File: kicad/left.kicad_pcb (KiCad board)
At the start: 4 copper layers, 137.5 x 109.3 mm, 114 parts, among them Q1 PMF170XP,115, Q2 FS8205A_C2830320, SW1 TS-1088-AR02016, U1 SN74LVC1G17DBVR, U2 E73-2G4M08S1C, U3 SN74LVC1G74DQER, U4 S2B-PH-K-S(LF)(SN), U5 BL8573CS8TR, U6 DW01A_C42380662, U7 LP5024RSMR, U8 MAX17048, U9 USBLC6-2SC6, X1 FC-13532.768KHZ9PF20PPM

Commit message: rewired and finalized right side. updated panel. changed dnp of some components on both sides
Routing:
- net /COL1: track 230.3 -> 227.1 mm
- net GND: vias 320 -> 340

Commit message: fixed u9 to have pin 5 after polyfuse
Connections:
- U9 pad 5: /VBUS_RAW -> /VBUS
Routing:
- net /VBUS: track 71.7 -> 83.0 mm
- net /VBUS_RAW: track 25.6 -> 17.2 mm

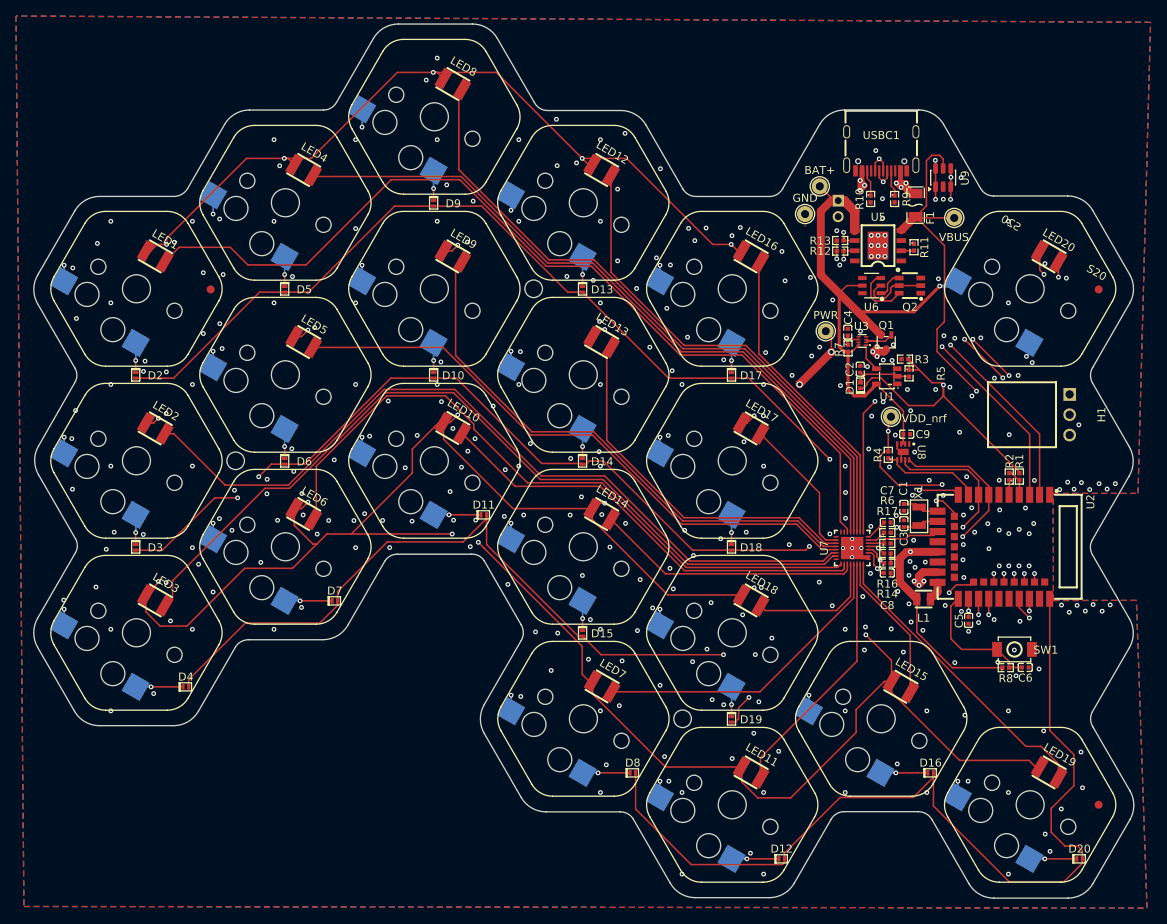
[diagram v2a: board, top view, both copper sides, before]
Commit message: plan for changing charger. reason = heat
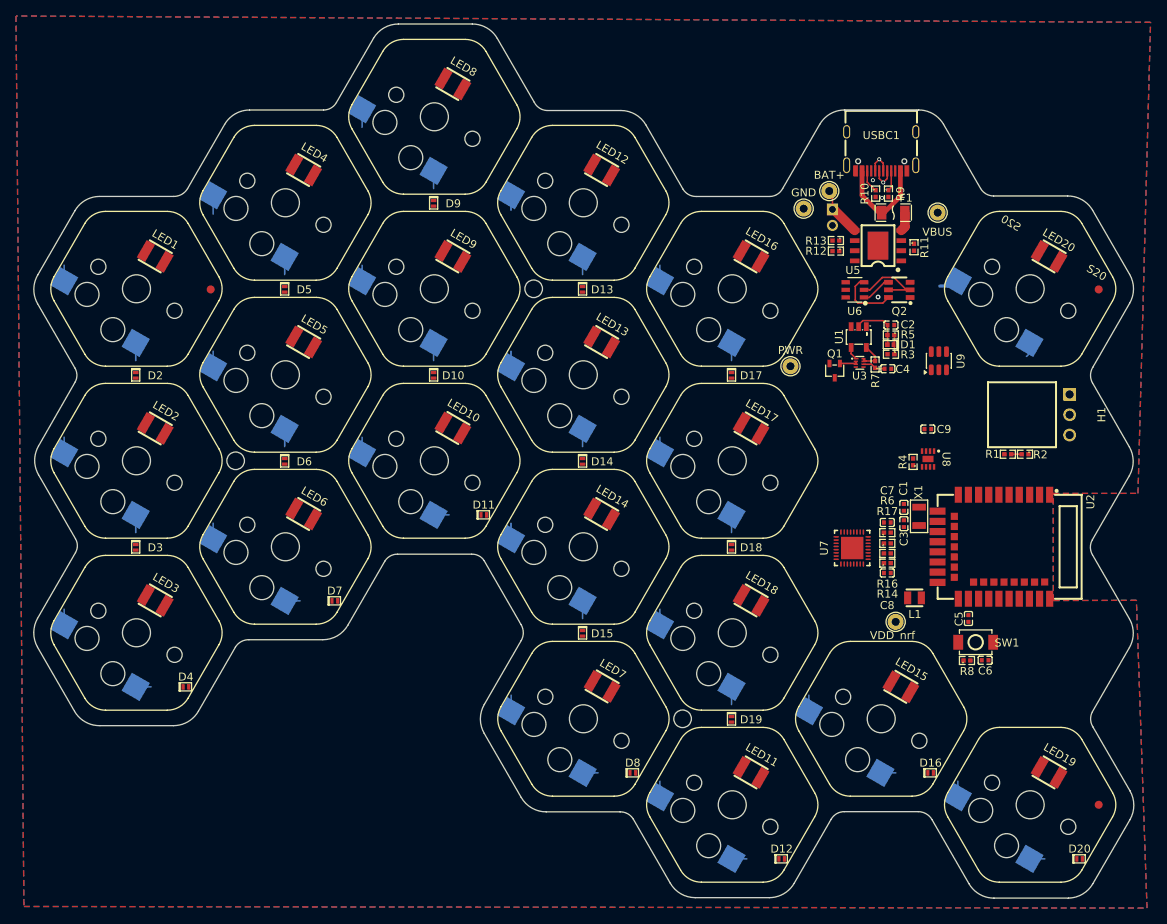
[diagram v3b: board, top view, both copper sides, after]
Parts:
- moved VDD_nrf 25.6 mm to (127.8, 90.5)
- moved U9 22.9 mm to (133.2, 57.9)
- moved Q1 7.35 mm to (120.2, 59.1)
- moved C4 6.78 mm to (126.8, 58.9), turned to 180 degrees
- moved C2 6.72 mm to (127.2, 53.4), turned to 0 degrees
- moved D1 6.30 mm to (127.1, 55.9), turned to 180 degrees
- moved PWR 6.22 mm to (114.6, 58.6)
- moved U1 6.04 mm to (123.2, 54.9), turned to 90 degrees
- moved R5 5.30 mm to (127.2, 54.7), turned to 180 degrees
- moved C6 5.09 mm to (139.0, 95.4)
- moved R8 4.94 mm to (136.7, 95.4)
- moved SW1 4.94 mm to (137.8, 93.1)
- moved R7 3.94 mm to (125.2, 58.4), turned to 90 degrees
- moved R2 3.42 mm to (144.0, 69.6), turned to 180 degrees
- moved U8 3.23 mm to (131.8, 70.2)
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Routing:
- net /PWR: track 701.5 -> 0.00 mm, vias 28 -> 0
- net /COL2: track 258.1 -> 8.36 mm, vias 5 -> 0
- net /COL3: track 233.2 -> 8.24 mm, vias 5 -> 0
- net /COL1: track 227.1 -> 6.00 mm, vias 4 -> 0
- net /COL4: track 196.2 -> 7.89 mm, vias 5 -> 0
- net /COL5: track 155.4 -> 8.00 mm, vias 5 -> 0
- net /ROW3: track 131.9 -> 0.00 mm, vias 3 -> 0
- net /ROW1: track 126.7 -> 0.00 mm, vias 2 -> 0
- net /ROW2: track 124.1 -> 0.00 mm, vias 4 -> 0
- net /ROW4: track 116.1 -> 0.00 mm
- net /LED1: track 114.9 -> 0.00 mm
- net /LED3: track 105.5 -> 0.00 mm
- net /LED2: track 100.9 -> 0.00 mm
- net /VDD_nRF: track 91.0 -> 0.00 mm, vias 4 -> 0
- net /LED4: track 90.8 -> 0.00 mm
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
